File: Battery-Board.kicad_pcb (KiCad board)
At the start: 2 copper layers, 100 x 100 mm, 180 parts, among them IC2 ESDALC6V1W5, J11 OLED, J12 USB_C_Receptacle_USB2.0_16P, J13 STM32-Prog-Header, Q1 CSD18563Q5A, Q2 CSD18563Q5A, SW3 RESET, SW4 SW_SPDT, U1 8MHz, U10 NTMFS4D0N08XT1G, U11 NTMFS4D0N08XT1G, U12 NTMFS4D0N08XT1G, U13 NTMFS4D0N08XT1G, U14 NTMFS4D0N08XT1G, U23 ACS723xLCTR-10AU, U24 ACS723xLCTR-10AU, U25 MCP6007, U26 MCP6007, U27 ACS723xLCTR-10AU, U28 MCP6007, U29 MCP6007, U3 STM32G491KEUx, U30 MCP6007, U31 MCP6007, U4 MCP2542FD-E/SN, U5 MCP9700AT-ETT, U6 MCP9700AT-ETT, U7 MCP9700AT-ETT, U8 LM5145, U9 LM5145

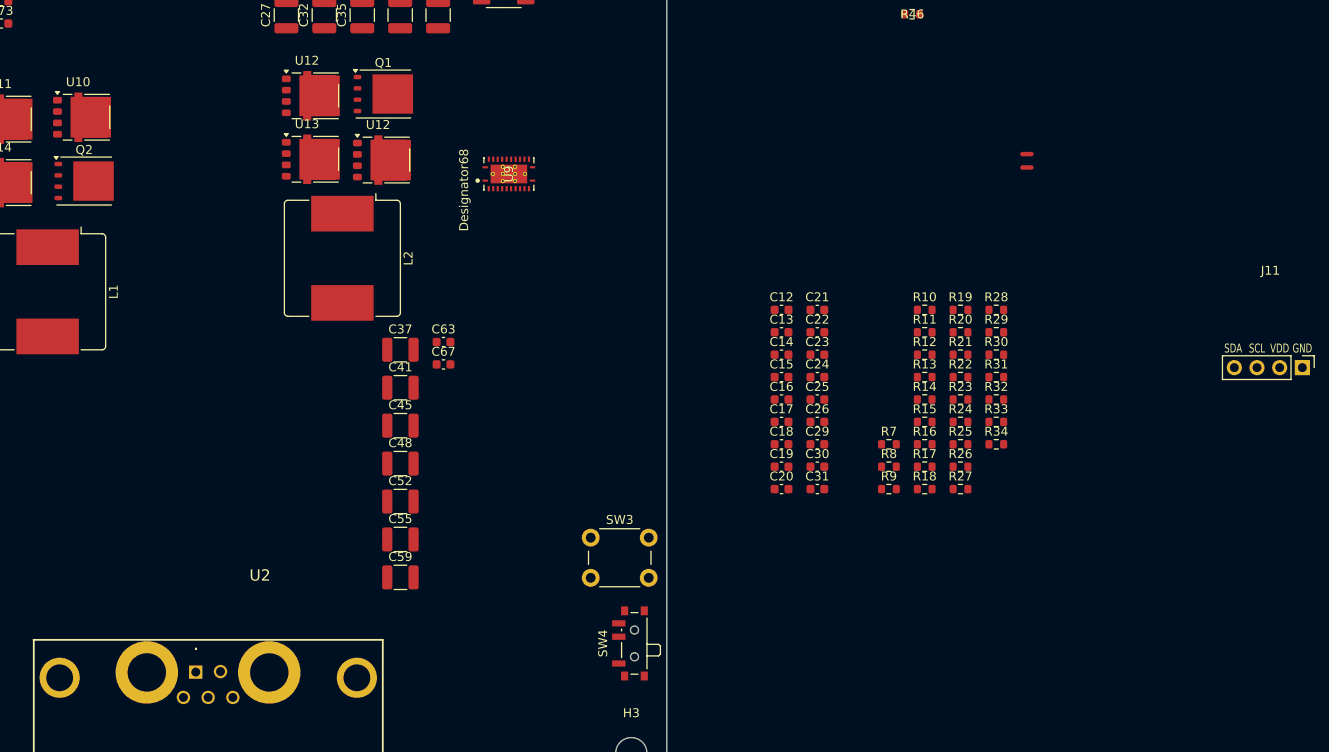
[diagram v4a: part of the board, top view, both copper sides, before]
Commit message: started sorting and cleaning up schemativc
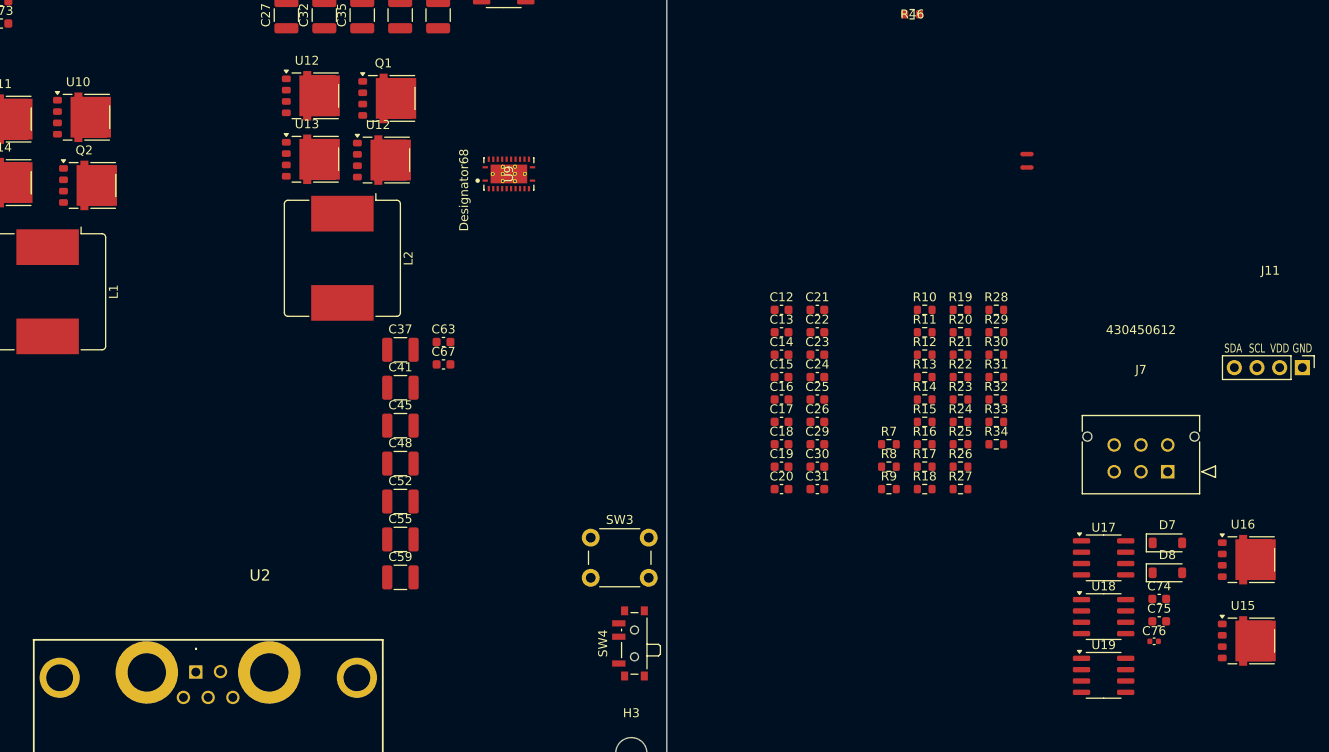
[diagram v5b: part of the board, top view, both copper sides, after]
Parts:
- added C74: 100n, Capacitor_SMD:C_0603_1608Metric, F.Cu at (243.0, 122.4)
- added C75: 1u5, Capacitor_SMD:C_0603_1608Metric, F.Cu at (243.0, 124.9)
- added C76: 1n, Capacitor_SMD:C_0402_1005Metric, F.Cu at (242.5, 127.2)
- added D7: MMSZ5226B-7-F, Diode_SMD:D_SOD-123, F.Cu at (244.0, 116.1)
- added D8: MMSZ5226B-7-F, Diode_SMD:D_SOD-123, F.Cu at (244.0, 119.5)
- added J7: STD_PWR_HEADER, ecocad_lib_footprints:CON_430450612_MOL, F.Cu at (244.0, 108.2)
- added U15: NTMFS4D0N08XT1G, ecocad_lib_footprints:PowerMosDFNHybrid, F.Cu at (252.4, 126.6)
- added U16: NTMFS4D0N08XT1G, ecocad_lib_footprints:PowerMosDFNHybrid, F.Cu at (252.4, 117.5)
- added U17: ACS723xLCTR-10AU, Package_SO:SOIC-8_3.9x4.9mm_P1.27mm, F.Cu at (236.8, 117.8)
- added U18: MCP6007, Package_SO:SOIC-8_3.9x4.9mm_P1.27mm, F.Cu at (236.8, 124.4)
- added U19: MCP6007, Package_SO:SOIC-8_3.9x4.9mm_P1.27mm, F.Cu at (236.8, 131.0)
- Q1, Q2: value CSD18563Q5A -> NTMFS4D0N08XT1G; footprint Package_TO_SOT_SMD:TDSON-8-1 -> ecocad_lib_footprints:PowerMosDFNHybrid
- R23: value 680 -> 680R
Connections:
- net /Power Circuitry/12V_Current_Out renamed /Power Sensors/12V_Current_Out
- net /Power Circuitry/12V_PCBs renamed /Power Sensors/12V_PCBs
- net /Power Circuitry/12V_Unsensed renamed /Power Sensors/12V_Unsensed
- net /Power Circuitry/7V_Current_Out renamed /Power Sensors/7V_Current_Out
- net /Power Circuitry/7V_PCBs renamed /Power Sensors/7V_PCBs
- net /Power Circuitry/7V_Unsensed renamed /Power Sensors/7V_Unsensed
- net /Power Circuitry/ADC_BUCK_12V_OUT renamed /Power Sensors/ADC_BUCK_12V_OUT
- net /Power Circuitry/ADC_BUCK_7V_Out renamed /Power Sensors/ADC_BUCK_7V_Out
- net /Power Circuitry/ADC_Battery_Voltage renamed /Power Sensors/ADC_Battery_Voltage
- net /Power Circuitry/Battery_Crrnt renamed /Power Sensors/Battery_Crrnt
- net /Power Circuitry/Battery_Terminal renamed /Power Sensors/Battery_Terminal
- net /Power Circuitry/Battery_Terminal_Unsensed renamed /Power Sensors/Battery_Terminal_Unsensed
- net /Power Circuitry/u11_unused renamed /Power Sensors/u11_unused
- net /Powerboard/SYNCOUT renamed /DC-DC-Converters/SYNCOUT
- net Net-(Q2-G) renamed /DC-DC-Converters/24V - 12V Converter/High Side Gate Drive
- net Net-(U11-G) renamed /DC-DC-Converters/24V - 12V Converter/Low Side Gate Drive
- C20 pad 1: GNDPWR -> GND
- C26 pad 2: GNDPWR -> GND
- C28 pad 1: +18.5V -> /DC-DC-Converters/24V - 12V Converter/POWER_IN
- C28 pad 2: GNDPWR -> GND
- C33 pad 1: +18.5V -> /DC-DC-Converters/24V - 12V Converter/POWER_IN
- C33 pad 2: GNDPWR -> GND
- C34 pad 1: Net-(C34-Pad1) -> /DC-DC-Converters/24V - 12V Converter/Output
- C34 pad 2: GNDPWR -> GND
- C36 pad 1: +18.5V -> /DC-DC-Converters/24V - 12V Converter/POWER_IN
- C36 pad 2: GNDPWR -> GND
- C38 pad 1: Net-(C34-Pad1) -> /DC-DC-Converters/24V - 12V Converter/Output
- C38 pad 2: GNDPWR -> GND
- C40 pad 1: +18.5V -> /DC-DC-Converters/24V - 12V Converter/POWER_IN
- C40 pad 2: GNDPWR -> GND
- C42 pad 1: Net-(C34-Pad1) -> /DC-DC-Converters/24V - 12V Converter/Output
- C42 pad 2: GNDPWR -> GND
- C44 pad 1: +18.5V -> /DC-DC-Converters/24V - 12V Converter/POWER_IN
- C44 pad 2: GNDPWR -> GND
- C46 pad 1: Net-(C34-Pad1) -> /DC-DC-Converters/24V - 12V Converter/Output
- C46 pad 2: GNDPWR -> GND
- C49 pad 1: +18.5V -> /DC-DC-Converters/24V - 12V Converter/POWER_IN
- C49 pad 2: GNDPWR -> GND
- C50 pad 1: Net-(C34-Pad1) -> /DC-DC-Converters/24V - 12V Converter/Output
- C50 pad 2: GNDPWR -> GND
- C53 pad 1: +18.5V -> /DC-DC-Converters/24V - 12V Converter/POWER_IN
- C53 pad 2: GNDPWR -> GND
- C54 pad 1: Net-(C34-Pad1) -> /DC-DC-Converters/24V - 12V Converter/Output
- C54 pad 2: GNDPWR -> GND
- C57 pad 1: Net-(C34-Pad1) -> /DC-DC-Converters/24V - 12V Converter/Output
- C57 pad 2: GNDPWR -> GND
- C58 pad 1: +18.5V -> /DC-DC-Converters/24V - 12V Converter/POWER_IN
- C58 pad 2: GNDPWR -> GND
- C61 pad 1: Net-(C34-Pad1) -> /DC-DC-Converters/24V - 12V Converter/Output
- C61 pad 2: GNDPWR -> GND
- C62 pad 1: +18.5V -> /DC-DC-Converters/24V - 12V Converter/POWER_IN
- C62 pad 2: GNDPWR -> GND
- C65 pad 1: Net-(C34-Pad1) -> /DC-DC-Converters/24V - 12V Converter/Output
- C65 pad 2: GNDPWR -> GND
- C66 pad 1: +18.5V -> /DC-DC-Converters/24V - 12V Converter/POWER_IN
- C66 pad 2: GNDPWR -> GND
- C69 pad 1: +18.5V -> /DC-DC-Converters/24V - 12V Converter/POWER_IN
- C69 pad 2: GNDPWR -> GND
- C71 pad 1: +18.5V -> /DC-DC-Converters/24V - 12V Converter/POWER_IN
- C71 pad 2: GNDPWR -> GND
- C73 pad 1: +18.5V -> /DC-DC-Converters/24V - 12V Converter/POWER_IN
- C73 pad 2: GNDPWR -> GND
- L1 pad 2: Net-(C34-Pad1) -> Net-(L1-Pad2)
- Q2 pad 1: +18.5V -> Net-(Q2-S-Pad1)
- Q2 pad 2: +18.5V -> Net-(Q2-S-Pad1)
- Q2 pad 3: +18.5V -> Net-(Q2-S-Pad1)
- R17 pad 1: +18.5V -> Net-(Q2-S-Pad1)
- R33 pad 2: Net-(C34-Pad1) -> Net-(L1-Pad2)
- R9 pad 1: +18.5V -> Net-(Q2-S-Pad1)
- U10 pad 1: +18.5V -> Net-(Q2-S-Pad1)
- U10 pad 2: +18.5V -> Net-(Q2-S-Pad1)
- U10 pad 3: +18.5V -> Net-(Q2-S-Pad1)
- U11 pad 5: GNDPWR -> GND
- U12 pad 1: (no net) -> +18.5V
- U12 pad 2: (no net) -> +18.5V
- U12 pad 3: (no net) -> +18.5V
- U12 pad 4: (no net) -> Net-(U12-G)
- U12 pad 5: (no net) -> Net-(Q1-D)
- U14 pad 5: GNDPWR -> GND

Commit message: Started Layout and cleaned up schematic
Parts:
- removed C43, C44, C46, C47, C49, C50, C51, C53, C54, C56, C57, C58: 10u, Capacitor_SMD:C_1210_3225Metric
- removed C45, C48, C52, C55, C59: 47u, Capacitor_SMD:C_1210_3225Metric
- removed C60, C62, C64, C66, C68, C69, C70, C71, C72, C73: 100n, Capacitor_SMD:C_0603_1608Metric
- removed C61, C63, C65, C67: 220u, Capacitor_SMD:C_0603_1608Metric
- removed D13, D14, D15, D16, D17, D18: MMSZ5226B-7-F, Diode_SMD:D_SOD-123
- removed FB2: 600@100MHz 1A, Inductor_SMD:L_0603_1608Metric
- removed IC2: ESDALC6V1W5, ecocad_lib_footprints:SOT65P210X110-5N
- removed J11: OLED, ecocad_lib_footprints:Display_128x64_096_I2C
- removed J12: USB_C_Receptacle_USB2.0_16P, Connector_USB:USB_C_Receptacle_GCT_USB4105-xx-A_16P_TopMnt_Horizontal
- removed J13: STM32-Prog-Header, ecocad_lib_footprints:IDC-STM32-Prog-Header_2x05_P2.54mm_Vertical
- removed J7: STD_PWR_HEADER, ecocad_lib_footprints:CON_430450612_MOL
- removed L2: 12u, ecocad_lib_footprints:L_Bourns_SRR1208_12.7x12.7mm
- removed NT1, NT2: NetTie_2, NetTie:NetTie-2_SMD_Pad0.5mm
- removed Q1, Q2, U13, U14, U15, U16: NTMFS4D0N08XT1G, ecocad_lib_footprints:PowerMosDFNHybrid
- removed R22: 0, Resistor_SMD:R_0603_1608Metric
- removed R23: 680R, Resistor_SMD:R_0603_1608Metric
- removed R24: 422, Resistor_SMD:R_0603_1608Metric
- removed R25: 3.83k, Resistor_SMD:R_0603_1608Metric
- removed R26: 3.3k, Resistor_SMD:R_0603_1608Metric
- removed R27, R28: 10k, Resistor_SMD:R_0603_1608Metric
- removed R29: 14k, Resistor_SMD:R_0603_1608Metric
- removed R30: 7.75k, Resistor_SMD:R_0603_1608Metric
- removed R31, R32: 1.00k, Resistor_SMD:R_0603_1608Metric
- removed R33, R34: 49.9, Resistor_SMD:R_0603_1608Metric
- removed SW3: RESET, Button_Switch_THT:SW_PUSH_6mm_H5mm
- removed SW4: SW_SPDT, Button_Switch_SMD:SW_SPDT_PCM12
- removed the U12 at (147.6, 65.6)
- removed the U12 at (155.5, 72.8)
- removed U24, U27: ACS723xLCTR-10AU, Package_SO:SOIC-8_3.9x4.9mm_P1.27mm
- removed U25, U26, U28, U29, U30, U31: MCP6007, Package_SO:SOIC-8_3.9x4.9mm_P1.27mm
- added C100: 15pF, Capacitor_SMD:C_0603_1608Metric, F.Cu at (111.2, 99.6)
- added C101: 150pF, Capacitor_SMD:C_0603_1608Metric, F.Cu at (118.5, 88.9)
- added C102: 100n, Capacitor_SMD:C_0603_1608Metric, F.Cu at (137.2, 101.8)
- added C104: 100n, Capacitor_SMD:C_0603_1608Metric, F.Cu at (135.6, 112.4)
- added C105: 1800pF, Capacitor_SMD:C_0603_1608Metric, F.Cu at (112.3, 88.9)
- added C106: 100n, Capacitor_SMD:C_0603_1608Metric, F.Cu at (134.1, 112.4)
- added C107: 100n, Capacitor_SMD:C_0603_1608Metric, F.Cu at (115.9, 99.0)
- added C77: 100n, Capacitor_SMD:C_0603_1608Metric, F.Cu at (78.3, 107.1)
- added C78: 10u, Capacitor_SMD:C_1210_3225Metric, F.Cu at (131.7, 101.0)
- added C79: 10u, Capacitor_SMD:C_1210_3225Metric, F.Cu at (131.5, 113.2)
- added C80: 100u, Capacitor_SMD:C_1210_3225Metric, F.Cu at (118.2, 119.5)
- added C81: 10u, Capacitor_SMD:C_1210_3225Metric, F.Cu at (128.2, 113.2)
- added C82: 1u, Capacitor_SMD:C_0603_1608Metric, F.Cu at (107.6, 85.8)
- added C83: 100n, Capacitor_SMD:C_0603_1608Metric, F.Cu at (122.3, 96.5)
- added C84: 100u, Capacitor_SMD:C_1210_3225Metric, F.Cu at (121.5, 119.5)
- added C97: 100n, Capacitor_SMD:C_0603_1608Metric, F.Cu at (135.7, 101.8)
- added C98: 5600pF, Capacitor_SMD:C_0603_1608Metric, F.Cu at (117.0, 88.9)
- added C99: 220u, ecocad_lib_footprints:CAP_EEE1HA221P, F.Cu at (104.5, 140.8)
- added FB1: 600@100MHz 1A, Inductor_SMD:L_0603_1608Metric, F.Cu at (58.2, 59.9)
- added IC1: ESDALC6V1W5, ecocad_lib_footprints:SOT65P210X110-5N, F.Cu at (24.6, 64.4)
- added J1: OLED, ecocad_lib_footprints:Display_128x64_096_I2C, F.Cu at (40.5, 30.5)
- added J2: USB_C_Receptacle_USB2.0_16P, Connector_USB:USB_C_Receptacle_GCT_USB4105-xx-A_16P_TopMnt_Horizontal, F.Cu at (172.0, 145.9)
- added J3: STM32-Prog-Header, Connector_PinHeader_2.54mm:PinHeader_2x05_P2.54mm_Vertical, F.Cu at (185.7, 56.1)
- added J4: Conn_01x01_Socket, Connector_PinHeader_2.54mm:PinHeader_1x01_P2.54mm_Vertical, F.Cu at (215.5, 86.5)
- added J5: Conn_01x01_Socket, Connector_PinHeader_2.54mm:PinHeader_1x01_P2.54mm_Vertical, F.Cu at (109.9, 82.2)
- added L3: 6u8, ecocad_lib_footprints:L_Bourns_SRR1208_12.7x12.7mm, F.Cu at (109.5, 121.6)
- added R36: 18.2k, Resistor_SMD:R_0603_1608Metric, F.Cu at (122.3, 91.9)
- added R37: 250k, Resistor_SMD:R_0603_1608Metric, F.Cu at (122.3, 93.5)
- added R38: 10k, Resistor_SMD:R_0603_1608Metric, F.Cu at (109.2, 88.9)
- added R39: 46.4k, Resistor_SMD:R_0603_1608Metric, F.Cu at (121.6, 88.9)
- added R40: 10k, Resistor_SMD:R_0603_1608Metric, F.Cu at (107.6, 88.9)
- added R49: 1.00k, Resistor_SMD:R_0603_1608Metric, F.Cu at (113.1, 86.6)
- added R50: 49.9, Resistor_SMD:R_0603_1608Metric, F.Cu at (113.1, 85.0)
- added SW1: RESET, Button_Switch_THT:SW_PUSH_6mm_H5mm, F.Cu at (56.1, 30.2)
- added SW2: SW_SPDT, Button_Switch_SMD:SW_SPDT_PCM12, F.Cu at (59.0, 39.7)
- added U12: MCP9700AT-ETT, Package_TO_SOT_SMD:SOT-23, F.Cu at (45.7, 67.8)
- added U20: NTMFS4D0N08XT1G, ecocad_lib_footprints:PowerMosDFNHybrid, F.Cu at (115.7, 109.8)
- added U21: NTMFS4D0N08XT1G, ecocad_lib_footprints:PowerMosDFNHybrid, F.Cu at (108.3, 109.8)
- added U22: NTMFS4D0N08XT1G, ecocad_lib_footprints:PowerMosDFNHybrid, F.Cu at (115.7, 103.4)
- C1, C15, C2, C85, C92: value 100n -> 10u; footprint Capacitor_SMD:C_0603_1608Metric -> Capacitor_SMD:C_1210_3225Metric
- C10, C14, C19, C7, C91, C96: value 100n -> 100u; footprint Capacitor_SMD:C_0603_1608Metric -> Capacitor_SMD:C_1210_3225Metric
- C11, C4, C8: value 0u1 -> 10u; footprint Capacitor_SMD:C_0603_1608Metric -> Capacitor_SMD:C_1210_3225Metric
- C12, C87: value 1u -> 100u; footprint Capacitor_SMD:C_0603_1608Metric -> Capacitor_SMD:C_1210_3225Metric
- C13: value 1u -> 10u; footprint Capacitor_SMD:C_0603_1608Metric -> Capacitor_SMD:C_1210_3225Metric
- C16: value 47n -> 10u; footprint Capacitor_SMD:C_0603_1608Metric -> Capacitor_SMD:C_1210_3225Metric
- C17: value 47n -> 100u; footprint Capacitor_SMD:C_0603_1608Metric -> Capacitor_SMD:C_1210_3225Metric
- C20: value 15pF -> 100n
- C21: value 15pF -> 5600pF
- C22: value 5600pF -> 220u; footprint Capacitor_SMD:C_0603_1608Metric -> ecocad_lib_footprints:CAP_EEE1HA221P
- C23: value 5600pF -> 15pF
- C25: value 150pF -> 100n
- C26: value 15n -> 220u; footprint Capacitor_SMD:C_0603_1608Metric -> ecocad_lib_footprints:CAP_EEE1HA221P
- C27, C32, C33, C38: value 10u -> 100n; footprint Capacitor_SMD:C_1210_3225Metric -> Capacitor_SMD:C_0603_1608Metric
- C28: value 10u -> 1800pF; footprint Capacitor_SMD:C_1210_3225Metric -> Capacitor_SMD:C_0603_1608Metric
- C29, C30: value 1800pF -> 100n
- C3: value 0u1 -> 100u; footprint Capacitor_SMD:C_0603_1608Metric -> Capacitor_SMD:C_1210_3225Metric
- C31: value C -> 220u; footprint Capacitor_SMD:C_0603_1608Metric -> ecocad_lib_footprints:CAP_EEE1HA221P
- C34, C35, C39, C42: value 10u -> 0u1; footprint Capacitor_SMD:C_1210_3225Metric -> Capacitor_SMD:C_0603_1608Metric
- C36: value 10u -> 4u7; footprint Capacitor_SMD:C_1210_3225Metric -> Capacitor_SMD:C_0603_1608Metric
- C37: value 47u -> 4u7; footprint Capacitor_SMD:C_1210_3225Metric -> Capacitor_SMD:C_0603_1608Metric
- C40: value 10u -> 1u; footprint Capacitor_SMD:C_1210_3225Metric -> Capacitor_SMD:C_0603_1608Metric
- C41: value 47u -> 100n; footprint Capacitor_SMD:C_1210_3225Metric -> Capacitor_SMD:C_0603_1608Metric
- C5: value 4u7 -> 1u
- C6: value 4u7 -> 100n
- C86: value 100n -> 47n
- C88: value 6.8u -> 10u; footprint Capacitor_SMD:C_0603_1608Metric -> Capacitor_SMD:C_1210_3225Metric
- C89, C94: value 1n -> 100u; footprint Capacitor_SMD:C_0402_1005Metric -> Capacitor_SMD:C_1210_3225Metric
- C9: value 1u -> 47n
- C90: value 1n -> 10u; footprint Capacitor_SMD:C_0402_1005Metric -> Capacitor_SMD:C_1210_3225Metric
- C93: value 1u5 -> 10u; footprint Capacitor_SMD:C_0603_1608Metric -> Capacitor_SMD:C_1210_3225Metric
- L1: value 6.8u -> 6u8
- R1: value 220R -> 18.2k; footprint Resistor_SMD:R_0805_2012Metric -> Resistor_SMD:R_0603_1608Metric
- R10: value 301k -> 3.83k
- R11: value 46.4k -> 10k
- R12: value 46.4k -> 0
- R13: value 20.0k -> 14k
- R14: value 20.0k -> 1.00k
- R15: value 20.0k -> 49.9
- R16: value 20.0k -> 220R; footprint Resistor_SMD:R_0603_1608Metric -> Resistor_SMD:R_0805_2012Metric
- R17: value 2.2 -> 220R; footprint Resistor_SMD:R_0603_1608Metric -> Resistor_SMD:R_0805_2012Metric
- R18: value 4.7 -> 220R; footprint Resistor_SMD:R_0603_1608Metric -> Resistor_SMD:R_0805_2012Metric
- R19: value 0 -> R
- R2: value 220R -> 250k; footprint Resistor_SMD:R_0805_2012Metric -> Resistor_SMD:R_0603_1608Metric
- R20, R21: value 0 -> 5.1k; footprint Resistor_SMD:R_0603_1608Metric -> Resistor_SMD:R_0805_2012Metric
- R3: value 220R -> 10k; footprint Resistor_SMD:R_0805_2012Metric -> Resistor_SMD:R_0603_1608Metric
- R4: value R -> 46.4k
- R41: value 28k7 -> 20.0k
- R42: value 10k -> 2.2
- R43: value 4k7 -> 680R
- R44: value 1k02 -> 0
- R45: value 13k6 -> 3.83k
- R46: value 4k7 -> 10k
- R47: value 47k -> 0; footprint Resistor_SMD:R_0805_2012Metric -> Resistor_SMD:R_0603_1608Metric
- R48: value 47k -> 14k; footprint Resistor_SMD:R_0805_2012Metric -> Resistor_SMD:R_0603_1608Metric
- R5: value 5.1k -> 10k; footprint Resistor_SMD:R_0805_2012Metric -> Resistor_SMD:R_0603_1608Metric
- R6: value 5.1k -> 20.0k; footprint Resistor_SMD:R_0805_2012Metric -> Resistor_SMD:R_0603_1608Metric
- R7: value 18.2k -> 2.2
- R8: value 18.2k -> 680R
- R9: value 250k -> 0
- U1: value 8MHz -> LM5145; footprint Crystal:Crystal_SMD_3225-4Pin_3.2x2.5mm -> Package_DFN_QFN:Texas_RGY_R-PVQFN-N20_EP2.05x3.05mm_ThermalVias
- U10, U11: value NTMFS4D0N08XT1G -> MCP9700AT-ETT; footprint ecocad_lib_footprints:PowerMosDFNHybrid -> Package_TO_SOT_SMD:SOT-23
- U19: value MCP6007 -> LM5145; footprint Package_SO:SOIC-8_3.9x4.9mm_P1.27mm -> Package_DFN_QFN:Texas_RGY_R-PVQFN-N20_EP2.05x3.05mm_ThermalVias
- U2: value ~ -> NTMFS4D0N08XT1G; footprint ecocad_lib_footprints:DB7W2-30A -> ecocad_lib_footprints:PowerMosDFNHybrid
- U23: value ACS723xLCTR-10AU -> NTMFS4D0N08XT1G; footprint Package_SO:SOIC-8_3.9x4.9mm_P1.27mm -> ecocad_lib_footprints:PowerMosDFNHybrid
- U3: value STM32G491KEUx -> NTMFS4D0N08XT1G; footprint Package_DFN_QFN:QFN-32-1EP_5x5mm_P0.5mm_EP3.45x3.45mm -> ecocad_lib_footprints:PowerMosDFNHybrid
- U4: value MCP2542FD-E/SN -> NTMFS4D0N08XT1G; footprint Package_SO:SOIC-8_3.9x4.9mm_P1.27mm -> ecocad_lib_footprints:PowerMosDFNHybrid
- U5: value MCP9700AT-ETT -> NTMFS4D0N08XT1G; footprint Package_TO_SOT_SMD:SOT-23 -> ecocad_lib_footprints:PowerMosDFNHybrid
- U6: value MCP9700AT-ETT -> 8MHz; footprint Package_TO_SOT_SMD:SOT-23 -> Crystal:Crystal_SMD_3225-4Pin_3.2x2.5mm
- U7: value MCP9700AT-ETT -> ~; footprint Package_TO_SOT_SMD:SOT-23 -> ecocad_lib_footprints:DB7W2-Female
- U8: value LM5145 -> STM32G491KEUx; footprint ecocad_lib_footprints:RGY0024F-MFG -> Package_DFN_QFN:QFN-32-1EP_5x5mm_P0.5mm_EP3.45x3.45mm
- U9: value LM5145 -> MCP2542FD-E/SN; footprint ecocad_lib_footprints:RGY0024F-MFG -> Package_SO:SOIC-8_3.9x4.9mm_P1.27mm
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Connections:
- C1 pad 1: GNDA -> /DC-DC-Converters/24V - 7V Converter/POWER_IN
- C1 pad 2: +3V3 -> GND
- C10 pad 1: GND -> /DC-DC-Converters/24V - 7V Converter/Output
- C10 pad 2: +3V3 -> GND
- C11 pad 1: +3V3 -> /DC-DC-Converters/24V - 7V Converter/POWER_IN
- C12 pad 1: GND -> /DC-DC-Converters/24V - 7V Converter/Output
- C12 pad 2: Net-(U8-VCC) -> GND
- C13 pad 1: GND -> /DC-DC-Converters/24V - 7V Converter/POWER_IN
- C13 pad 2: Net-(U9-VCC) -> GND
- C14 pad 1: GNDPWR -> /DC-DC-Converters/24V - 7V Converter/Output
- C14 pad 2: Net-(U8-VIN) -> GND
- C15 pad 1: GNDPWR -> /DC-DC-Converters/24V - 7V Converter/POWER_IN
- C15 pad 2: Net-(U9-VIN) -> GND
- C16 pad 1: GND -> /DC-DC-Converters/24V - 7V Converter/POWER_IN
- C16 pad 2: Net-(U8-SS_TRK) -> GND
- C17 pad 1: GND -> /DC-DC-Converters/24V - 7V Converter/Output
- C17 pad 2: Net-(U9-SS_TRK) -> GND
- C18 pad 1: Net-(Q2-D) -> /DC-DC-Converters/24V - 7V Converter/POWER_IN
- C18 pad 2: Net-(Q2-D) -> GND
- C19 pad 1: Net-(Q1-D) -> /DC-DC-Converters/24V - 7V Converter/Output
- C19 pad 2: Net-(Q1-D) -> GND
- C2 pad 1: GND -> /DC-DC-Converters/24V - 7V Converter/POWER_IN
- C2 pad 2: /MCU and sensors/NRST -> GND
- C20 pad 1: GND -> /DC-DC-Converters/24V - 7V Converter/POWER_IN
- C20 pad 2: Net-(U8-ILIM) -> GND
- C21 pad 1: GNDPWR -> Net-(U1-COMP)
- C21 pad 2: Net-(U9-ILIM) -> Net-(C21-Pad2)
- C22 pad 1: Net-(U8-COMP) -> /DC-DC-Converters/24V - 7V Converter/Output
- C22 pad 2: Net-(C22-Pad2) -> GND
- C23 pad 1: Net-(U9-COMP) -> GND
- C23 pad 2: Net-(C23-Pad2) -> Net-(U1-ILIM)
- C24 pad 1: Net-(U8-COMP) -> Net-(U1-COMP)
- C24 pad 2: Net-(U8-FB) -> Net-(U1-FB)
- C25 pad 1: Net-(U9-COMP) -> /DC-DC-Converters/24V - 7V Converter/POWER_IN
- C25 pad 2: Net-(U9-FB) -> GND
- C26 pad 1: Net-(Q2-D) -> /DC-DC-Converters/24V - 7V Converter/Output
- C27 pad 1: +18.5V -> /DC-DC-Converters/24V - 7V Converter/POWER_IN
- C27 pad 2: GNDPWR -> GND
- C28 pad 1: /DC-DC-Converters/24V - 12V Converter/POWER_IN -> Net-(U1-FB)
- C28 pad 2: GND -> Net-(C28-Pad2)
- C29 pad 1: Net-(U8-FB) -> /DC-DC-Converters/24V - 7V Converter/POWER_IN
- C29 pad 2: Net-(C29-Pad2) -> GND
- C3 pad 1: +3V3 -> /DC-DC-Converters/24V - 7V Converter/Output
- C3 pad 2: GNDA -> GND
- C30 pad 1: Net-(U9-FB) -> Net-(U1-SW)
- C30 pad 2: Net-(C30-Pad2) -> Net-(U1-BST)
- C31 pad 1: Net-(Q1-D) -> /DC-DC-Converters/24V - 12V Converter/Output
- C31 pad 2: GNDPWR -> GND
- C32 pad 1: +18.5V -> GNDA
- C32 pad 2: GNDPWR -> +3V3
- C33 pad 1: /DC-DC-Converters/24V - 12V Converter/POWER_IN -> GND
- C33 pad 2: GND -> /MCU and sensors/NRST
- C34 pad 1: /DC-DC-Converters/24V - 12V Converter/Output -> +3V3
- C34 pad 2: GND -> GNDA
- C35 pad 1: +18.5V -> +3V3
- C35 pad 2: GNDPWR -> GNDA
- C36 pad 1: /DC-DC-Converters/24V - 12V Converter/POWER_IN -> +3V3
- C36 pad 2: GND -> GNDA
- C37 pad 1: Net-(C37-Pad1) -> +3.3VA
- C37 pad 2: GNDPWR -> unconnected-(C37-Pad2)
- C38 pad 1: /DC-DC-Converters/24V - 12V Converter/Output -> GND
- C38 pad 2: GND -> +5V
- C39 pad 1: +18.5V -> +3.3VA
- C39 pad 2: GNDPWR -> GND
- C4 pad 1: +3V3 -> /DC-DC-Converters/24V - 7V Converter/POWER_IN
- C4 pad 2: GNDA -> GND
- C40 pad 1: /DC-DC-Converters/24V - 12V Converter/POWER_IN -> +3.3VA
- C41 pad 1: Net-(C37-Pad1) -> GND
- C41 pad 2: GNDPWR -> +3V3
- C42 pad 1: /DC-DC-Converters/24V - 12V Converter/Output -> +3V3
- C5 pad 1: +3V3 -> GND
- C5 pad 2: GNDA -> Net-(U1-VCC)
- C6 pad 1: +3.3VA -> GND
- C6 pad 2: unconnected-(C6-Pad2) -> Net-(U1-VIN)
- C7 pad 1: GND -> /DC-DC-Converters/24V - 7V Converter/Output
- C7 pad 2: +5V -> GND
- C74 pad 2: GND -> /Power Sensor VI/SENSOR_GND
- C8 pad 1: +3.3VA -> /DC-DC-Converters/24V - 7V Converter/POWER_IN
- C85 pad 1: +5V -> /DC-DC-Converters/24V - 12V Converter/POWER_IN
- C86 pad 2: +5V -> Net-(U19-SS_TRK)
- C87 pad 1: Net-(D13-K) -> /DC-DC-Converters/24V - 12V Converter/Output
- C88 pad 1: Net-(D14-K) -> /DC-DC-Converters/24V - 12V Converter/POWER_IN
- C89 pad 1: Net-(D15-K) -> /DC-DC-Converters/24V - 12V Converter/Output
- C9 pad 1: +3.3VA -> GND
- C9 pad 2: GND -> Net-(U1-SS_TRK)
- C90 pad 1: Net-(D16-K) -> /DC-DC-Converters/24V - 12V Converter/POWER_IN
- C91 pad 1: +5V -> /DC-DC-Converters/24V - 12V Converter/Output
- C92 pad 1: +5V -> /DC-DC-Converters/24V - 12V Converter/POWER_IN
- C93 pad 1: Net-(D17-K) -> /DC-DC-Converters/24V - 12V Converter/POWER_IN
- C94 pad 1: Net-(D18-K) -> /DC-DC-Converters/24V - 12V Converter/Output
- C95 pad 1: +5V -> /DC-DC-Converters/24V - 12V Converter/POWER_IN
- C96 pad 1: +5V -> /DC-DC-Converters/24V - 12V Converter/Output
- L1 pad 1: Net-(Q2-D) -> Net-(U1-SW)
- L1 pad 2: Net-(L1-Pad2) -> /DC-DC-Converters/24V - 7V Converter/Output
- R1 pad 1: Net-(D1-A) -> GND
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
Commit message: A
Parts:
- added C43: 100u, Capacitor_SMD:C_1210_3225Metric, F.Cu at (236.8, 133.8)
- added C44: 100u, Capacitor_SMD:C_1210_3225Metric, B.Cu at (118.1, 119.5)
- C1, C11, C13, C15, C16, C2, C4, C78, C79, C8, C81, C85, C88, C90, C92, C93: value 10u -> 100u
- C91, C94, C96: moved to B.Cu
- moved C96 16.6 mm to (121.4, 119.5)
- moved C94 9.93 mm to (124.8, 119.5)
- moved C91 3.32 mm to (128.1, 119.5)

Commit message: A
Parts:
- removed C100: 15pF, Capacitor_SMD:C_0603_1608Metric
- removed C101: 150pF, Capacitor_SMD:C_0603_1608Metric
- removed C102, C104, C106, C107, C95, C97: 100n, Capacitor_SMD:C_0603_1608Metric
- removed C105: 1800pF, Capacitor_SMD:C_0603_1608Metric
- removed C94, C96: 100u, Capacitor_SMD:C_1210_3225Metric
- removed C98: 5600pF, Capacitor_SMD:C_0603_1608Metric
- removed C99: 220u, ecocad_lib_footprints:CAP_EEE1HA221P
- removed L3: 6u8, ecocad_lib_footprints:L_Bourns_SRR1208_12.7x12.7mm
- removed R36: 18.2k, Resistor_SMD:R_0603_1608Metric
- removed R37: 250k, Resistor_SMD:R_0603_1608Metric
- removed R38, R40, R46: 10k, Resistor_SMD:R_0603_1608Metric
- removed R39: 46.4k, Resistor_SMD:R_0603_1608Metric
- removed R41: 20.0k, Resistor_SMD:R_0603_1608Metric
- removed R42: 2.2, Resistor_SMD:R_0603_1608Metric
- removed R43: 680R, Resistor_SMD:R_0603_1608Metric
- removed R44, R47: 0, Resistor_SMD:R_0603_1608Metric
- removed R45: 3.83k, Resistor_SMD:R_0603_1608Metric
- removed R48: 14k, Resistor_SMD:R_0603_1608Metric
- removed R49: 1.00k, Resistor_SMD:R_0603_1608Metric
- removed R50: 49.9, Resistor_SMD:R_0603_1608Metric
- added C45: 100n, Capacitor_SMD:C_0603_1608Metric, F.Cu at (18.9, 117.2)
- added C46: 220u, ecocad_lib_footprints:CAP_EEE1HA221P, F.Cu at (24.1, 136.9)
- added C47: 100n, Capacitor_SMD:C_0603_1608Metric, F.Cu at (18.9, 119.7)
- added C48: 1800pF, Capacitor_SMD:C_0603_1608Metric, F.Cu at (18.9, 122.2)
- added C49: 100n, Capacitor_SMD:C_0603_1608Metric, F.Cu at (18.9, 124.7)
- added C50: 100n, Capacitor_SMD:C_0603_1608Metric, F.Cu at (18.9, 127.2)
- added C51: 100n, Capacitor_SMD:C_0603_1608Metric, F.Cu at (49.9, 85.9)
- added C52: 1u5, Capacitor_SMD:C_0603_1608Metric, F.Cu at (49.9, 88.4)
- added C53: 1n, Capacitor_SMD:C_0402_1005Metric, F.Cu at (53.4, 92.3)
- added C54: 100n, Capacitor_SMD:C_0603_1608Metric, F.Cu at (49.9, 90.9)
- added C55: 100u, Capacitor_SMD:C_1210_3225Metric, F.Cu at (11.7, 86.7)
- added C56: 100u, Capacitor_SMD:C_1210_3225Metric, F.Cu at (11.7, 91.0)
- added C57: 100u, Capacitor_SMD:C_1210_3225Metric, F.Cu at (11.7, 95.2)
- added C58: 100u, Capacitor_SMD:C_1210_3225Metric, F.Cu at (11.7, 99.5)
- added C59: 100u, Capacitor_SMD:C_1210_3225Metric, F.Cu at (11.7, 103.7)
- added C60: 1u, Capacitor_SMD:C_0603_1608Metric, F.Cu at (27.8, 100.1)
- added C61: 100n, Capacitor_SMD:C_0603_1608Metric, F.Cu at (27.8, 102.6)
- added C62: 100u, Capacitor_SMD:C_1210_3225Metric, F.Cu at (11.7, 108.0)
- added C63: 100u, Capacitor_SMD:C_1210_3225Metric, F.Cu at (17.4, 86.7)
- added C64: 47n, Capacitor_SMD:C_0603_1608Metric, F.Cu at (27.8, 105.1)
- added C65: 100u, Capacitor_SMD:C_1210_3225Metric, F.Cu at (17.4, 91.0)
- added C66: 100u, Capacitor_SMD:C_1210_3225Metric, F.Cu at (17.4, 95.2)
- added C67: 100u, Capacitor_SMD:C_1210_3225Metric, F.Cu at (17.4, 99.5)
- added C68: 100u, Capacitor_SMD:C_1210_3225Metric, F.Cu at (17.4, 103.7)
- added C69: 100u, Capacitor_SMD:C_1210_3225Metric, F.Cu at (17.4, 108.0)
- added C70: 100u, Capacitor_SMD:C_1210_3225Metric, F.Cu at (23.0, 86.7)
- added C71: 100u, Capacitor_SMD:C_1210_3225Metric, F.Cu at (23.0, 91.0)
- added C72: 100u, Capacitor_SMD:C_1210_3225Metric, F.Cu at (23.0, 95.2)
- added C73: 100n, Capacitor_SMD:C_0603_1608Metric, F.Cu at (27.8, 107.6)
- added D10: MMSZ5226B-7-F, Diode_SMD:D_SOD-123, F.Cu at (50.8, 100.3)
- added D11: MMSZ5226B-7-F, Diode_SMD:D_SOD-123, F.Cu at (54.8, 86.3)
- added D12: MMSZ5226B-7-F, Diode_SMD:D_SOD-123, F.Cu at (54.8, 89.6)
- added D13: MMSZ5226B-7-F, Diode_SMD:D_SOD-123, F.Cu at (44.6, 117.6)
- added D14: MMSZ5226B-7-F, Diode_SMD:D_SOD-123, F.Cu at (44.6, 120.9)
- added D15: MMSZ5226B-7-F, Diode_SMD:D_SOD-123, F.Cu at (44.6, 132.8)
- added D16: MMSZ5226B-7-F, Diode_SMD:D_SOD-123, F.Cu at (44.6, 136.1)
- added D9: MMSZ5226B-7-F, Diode_SMD:D_SOD-123, F.Cu at (50.8, 97.0)
- added G***: LOGO, LOGO, F.Cu at (107.0, 68.6)
- added G***: LOGO, LOGO, F.Cu at (135.7, 116.6)
- added G***: LOGO, LOGO, F.Cu at (155.7, 79.0)
- added L2: 6u8, ecocad_lib_footprints:L_Bourns_SRR1208_12.7x12.7mm, F.Cu at (33.6, 91.7)
- added R22: 1.00k, Resistor_SMD:R_0603_1608Metric, F.Cu at (18.9, 129.7)
- added R23: 18.2k, Resistor_SMD:R_0603_1608Metric, F.Cu at (27.8, 110.2)
- added R24: 250k, Resistor_SMD:R_0603_1608Metric, F.Cu at (27.8, 112.7)
- added R25: 10k, Resistor_SMD:R_0603_1608Metric, F.Cu at (31.8, 100.1)
- added R26: 46.4k, Resistor_SMD:R_0603_1608Metric, F.Cu at (31.8, 102.6)
- added R27: 10k, Resistor_SMD:R_0603_1608Metric, F.Cu at (31.8, 105.1)
- added R28: 20.0k, Resistor_SMD:R_0603_1608Metric, F.Cu at (31.8, 107.6)
- added R29: 2.2, Resistor_SMD:R_0603_1608Metric, F.Cu at (31.8, 110.2)
- added R30: 680R, Resistor_SMD:R_0603_1608Metric, F.Cu at (31.8, 112.7)
- added R31: 0, Resistor_SMD:R_0603_1608Metric, F.Cu at (35.9, 100.1)
- added R32: 10k, Resistor_SMD:R_0603_1608Metric, F.Cu at (35.9, 102.6)
- added R33: 0, Resistor_SMD:R_0603_1608Metric, F.Cu at (35.9, 105.1)
- added R34: 1.00k, Resistor_SMD:R_0603_1608Metric, F.Cu at (35.9, 107.6)
- added U13: NTMFS4D0N08XT1G, ecocad_lib_footprints:PowerMosDFNHybrid, F.Cu at (12.5, 119.0)
- added U14: NTMFS4D0N08XT1G, ecocad_lib_footprints:PowerMosDFNHybrid, F.Cu at (12.5, 126.1)
- added U15: NTMFS4D0N08XT1G, ecocad_lib_footprints:PowerMosDFNHybrid, F.Cu at (12.5, 133.2)
- added U16: NTMFS4D0N08XT1G, ecocad_lib_footprints:PowerMosDFNHybrid, F.Cu at (12.5, 140.3)
- added U24: NTMFS4D0N08XT1G, ecocad_lib_footprints:PowerMosDFNHybrid, F.Cu at (41.5, 101.9)
- added U25: NTMFS4D0N08XT1G, ecocad_lib_footprints:PowerMosDFNHybrid, F.Cu at (41.5, 109.0)
- added U26: ACS723xLCTR-10AU, Package_SO:SOIC-8_3.9x4.9mm_P1.27mm, F.Cu at (37.5, 119.3)
- added U27: MCP6007, Package_SO:SOIC-8_3.9x4.9mm_P1.27mm, F.Cu at (37.5, 125.8)
- added U28: ACS723xLCTR-10AU, Package_SO:SOIC-8_3.9x4.9mm_P1.27mm, F.Cu at (37.5, 134.4)
- added U29: MCP6007, Package_SO:SOIC-8_3.9x4.9mm_P1.27mm, F.Cu at (37.5, 141.0)
- C1, C11, C14, C16, C19, C4, C80, C84, C85, C89, C90, C93: value 100u -> 100n; footprint Capacitor_SMD:C_1210_3225Metric -> Capacitor_SMD:C_0603_1608Metric
- C10: value 100u -> 4u7; footprint Capacitor_SMD:C_1210_3225Metric -> Capacitor_SMD:C_0603_1608Metric
- C12, C15, C7, C8: value 100u -> 0u1; footprint Capacitor_SMD:C_1210_3225Metric -> Capacitor_SMD:C_0603_1608Metric
- C13: value 100u -> 1u; footprint Capacitor_SMD:C_1210_3225Metric -> Capacitor_SMD:C_0603_1608Metric
- C17, C2, C87, C91: value 100u -> 1u5; footprint Capacitor_SMD:C_1210_3225Metric -> Capacitor_SMD:C_0603_1608Metric
- C18: value 100n -> 1n; footprint Capacitor_SMD:C_0603_1608Metric -> Capacitor_SMD:C_0402_1005Metric
- C20, C27, C30, C32, C33, C74: value 100n -> 100u; footprint Capacitor_SMD:C_0603_1608Metric -> Capacitor_SMD:C_1210_3225Metric
- C21: value 5600pF -> 100u; footprint Capacitor_SMD:C_0603_1608Metric -> Capacitor_SMD:C_1210_3225Metric
- C22, C31: value 220u -> 100u; footprint ecocad_lib_footprints:CAP_EEE1HA221P -> Capacitor_SMD:C_1210_3225Metric
- C23: value 15pF -> 100u; footprint Capacitor_SMD:C_0603_1608Metric -> Capacitor_SMD:C_1210_3225Metric
- C24: value 150pF -> 100u; footprint Capacitor_SMD:C_0603_1608Metric -> Capacitor_SMD:C_1210_3225Metric
- C25: value 100n -> 1u
- C26: value 220u -> 100n; footprint ecocad_lib_footprints:CAP_EEE1HA221P -> Capacitor_SMD:C_0603_1608Metric
- C28: value 1800pF -> 100u; footprint Capacitor_SMD:C_0603_1608Metric -> Capacitor_SMD:C_1210_3225Metric
- C29: value 100n -> 47n
- C3, C88, C92: value 100u -> 1n; footprint Capacitor_SMD:C_1210_3225Metric -> Capacitor_SMD:C_0402_1005Metric
- C34, C35, C39: value 0u1 -> 100u; footprint Capacitor_SMD:C_0603_1608Metric -> Capacitor_SMD:C_1210_3225Metric
- C36, C37: value 4u7 -> 100u; footprint Capacitor_SMD:C_0603_1608Metric -> Capacitor_SMD:C_1210_3225Metric
- C40: value 1u -> 5600pF
- C42: value 0u1 -> 220u; footprint Capacitor_SMD:C_0603_1608Metric -> ecocad_lib_footprints:CAP_EEE1HA221P
- C43, C78: value 100u -> 150pF; footprint Capacitor_SMD:C_1210_3225Metric -> Capacitor_SMD:C_0603_1608Metric
- C44, C79: value 100u -> 15pF; footprint Capacitor_SMD:C_1210_3225Metric -> Capacitor_SMD:C_0603_1608Metric
- C5, C82: value 1u -> 100n
- C75: value 1u5 -> 5600pF
- C76: value 1n -> 100n; footprint Capacitor_SMD:C_0402_1005Metric -> Capacitor_SMD:C_0603_1608Metric
- C77: value 100n -> 220u; footprint Capacitor_SMD:C_0603_1608Metric -> ecocad_lib_footprints:CAP_EEE1HA221P
- C81: value 100u -> 220u; footprint Capacitor_SMD:C_1210_3225Metric -> ecocad_lib_footprints:CAP_EEE1HA221P
- C83: value 100n -> 1800pF
- C86: value 47n -> 100n
- C9: value 47n -> 4u7
- D1: value AMBER -> MMSZ5226B-7-F; footprint LED_SMD:LED_0805_2012Metric -> Diode_SMD:D_SOD-123
- D2: value RED -> MMSZ5226B-7-F; footprint LED_SMD:LED_0805_2012Metric -> Diode_SMD:D_SOD-123
- D3: value GREEN -> AMBER
- D4: value MMSZ5226B-7-F -> RED; footprint Diode_SMD:D_SOD-123 -> LED_SMD:LED_0805_2012Metric
- D5: value USBLC6-2SC6 -> GREEN; footprint Package_TO_SOT_SMD:TSOT-23-6_HandSoldering -> LED_SMD:LED_0805_2012Metric
- D6: value MMSZ5231B-7-F -> MMSZ5226B-7-F
- D7: value MMSZ5226B-7-F -> USBLC6-2SC6; footprint Diode_SMD:D_SOD-123 -> Package_TO_SOT_SMD:TSOT-23-6_HandSoldering
- D8: value MMSZ5226B-7-F -> MMSZ5231B-7-F
- R1: value 18.2k -> 220R; footprint Resistor_SMD:R_0603_1608Metric -> Resistor_SMD:R_0805_2012Metric
- R11: value 10k -> 18.2k
- R12: value 0 -> 250k
- R13: value 14k -> 10k
- R14: value 1.00k -> 46.4k
- R15: value 49.9 -> 10k
- R16: value 220R -> 20.0k; footprint Resistor_SMD:R_0805_2012Metric -> Resistor_SMD:R_0603_1608Metric
- R17: value 220R -> 2.2; footprint Resistor_SMD:R_0805_2012Metric -> Resistor_SMD:R_0603_1608Metric
- R18: value 220R -> 680R; footprint Resistor_SMD:R_0805_2012Metric -> Resistor_SMD:R_0603_1608Metric
- R19: value R -> 0
- R2: value 250k -> 220R; footprint Resistor_SMD:R_0603_1608Metric -> Resistor_SMD:R_0805_2012Metric
- R20: value 5.1k -> 10k; footprint Resistor_SMD:R_0805_2012Metric -> Resistor_SMD:R_0603_1608Metric
- R21: value 5.1k -> 0; footprint Resistor_SMD:R_0805_2012Metric -> Resistor_SMD:R_0603_1608Metric
- R3: value 10k -> 220R; footprint Resistor_SMD:R_0603_1608Metric -> Resistor_SMD:R_0805_2012Metric
- R4: value 46.4k -> R
- R5: value 10k -> 5.1k; footprint Resistor_SMD:R_0603_1608Metric -> Resistor_SMD:R_0805_2012Metric
- R6: value 20.0k -> 5.1k; footprint Resistor_SMD:R_0603_1608Metric -> Resistor_SMD:R_0805_2012Metric
- U1: value LM5145 -> ACS723xLCTR-10AU; footprint Package_DFN_QFN:Texas_RGY_R-PVQFN-N20_EP2.05x3.05mm_ThermalVias -> Package_SO:SOIC-8_3.9x4.9mm_P1.27mm
- U10: value MCP9700AT-ETT -> ACS723xLCTR-10AU; footprint Package_TO_SOT_SMD:SOT-23 -> Package_SO:SOIC-8_3.9x4.9mm_P1.27mm
- U11: value MCP9700AT-ETT -> MCP6007; footprint Package_TO_SOT_SMD:SOT-23 -> Package_SO:SOIC-8_3.9x4.9mm_P1.27mm
- U12: value MCP9700AT-ETT -> LM5145; footprint Package_TO_SOT_SMD:SOT-23 -> Package_DFN_QFN:Texas_RGY_R-PVQFN-N20_EP2.05x3.05mm_ThermalVias
- U19: value LM5145 -> MCP6007; footprint Package_DFN_QFN:Texas_RGY_R-PVQFN-N20_EP2.05x3.05mm_ThermalVias -> Package_SO:SOIC-8_3.9x4.9mm_P1.27mm
- U2, U20: value NTMFS4D0N08XT1G -> MCP6007; footprint ecocad_lib_footprints:PowerMosDFNHybrid -> Package_SO:SOIC-8_3.9x4.9mm_P1.27mm
- U21: value NTMFS4D0N08XT1G -> LM5145; footprint ecocad_lib_footprints:PowerMosDFNHybrid -> Package_DFN_QFN:Texas_RGY_R-PVQFN-N20_EP2.05x3.05mm_ThermalVias
- U3: value NTMFS4D0N08XT1G -> 8MHz; footprint ecocad_lib_footprints:PowerMosDFNHybrid -> Crystal:Crystal_SMD_3225-4Pin_3.2x2.5mm
- U4: value NTMFS4D0N08XT1G -> ~; footprint ecocad_lib_footprints:PowerMosDFNHybrid -> ecocad_lib_footprints:DB7W2-Female
- U5: value NTMFS4D0N08XT1G -> STM32G491KEUx; footprint ecocad_lib_footprints:PowerMosDFNHybrid -> Package_DFN_QFN:QFN-32-1EP_5x5mm_P0.5mm_EP3.45x3.45mm
- U6: value 8MHz -> MCP2542FD-E/SN; footprint Crystal:Crystal_SMD_3225-4Pin_3.2x2.5mm -> Package_SO:SOIC-8_3.9x4.9mm_P1.27mm
- U7: value ~ -> MCP9700AT-ETT; footprint ecocad_lib_footprints:DB7W2-Female -> Package_TO_SOT_SMD:SOT-23
- U8: value STM32G491KEUx -> MCP9700AT-ETT; footprint Package_DFN_QFN:QFN-32-1EP_5x5mm_P0.5mm_EP3.45x3.45mm -> Package_TO_SOT_SMD:SOT-23
- U9: value MCP2542FD-E/SN -> MCP9700AT-ETT; footprint Package_SO:SOIC-8_3.9x4.9mm_P1.27mm -> Package_TO_SOT_SMD:SOT-23
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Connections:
- C1 pad 1: /DC-DC-Converters/24V - 7V Converter/POWER_IN -> /DC-DC-Converters/Power Sensor VI1/SENSOR_VCC
- C1 pad 2: GND -> /DC-DC-Converters/Power Sensor VI1/SENSOR_GND
- C10 pad 1: /DC-DC-Converters/24V - 7V Converter/Output -> +3.3VA
- C10 pad 2: GND -> unconnected-(C10-Pad2)
- C11 pad 1: /DC-DC-Converters/24V - 7V Converter/POWER_IN -> GND
- C11 pad 2: GND -> +5V
- C12 pad 1: /DC-DC-Converters/24V - 7V Converter/Output -> +3.3VA
- C13 pad 1: /DC-DC-Converters/24V - 7V Converter/POWER_IN -> +3.3VA
- C14 pad 1: /DC-DC-Converters/24V - 7V Converter/Output -> GND
- C14 pad 2: GND -> +3V3
- C15 pad 1: /DC-DC-Converters/24V - 7V Converter/POWER_IN -> +3V3
- C16 pad 1: /DC-DC-Converters/24V - 7V Converter/POWER_IN -> /DC-DC-Converters/Power Sensor VI2/SENSOR_VCC
- C16 pad 2: GND -> /DC-DC-Converters/Power Sensor VI2/SENSOR_GND
- C17 pad 1: /DC-DC-Converters/24V - 7V Converter/Output -> /DC-DC-Converters/OUT_{12V}
- C17 pad 2: GND -> /DC-DC-Converters/Power Sensor VI2/SENSOR_GND
- C18 pad 1: /DC-DC-Converters/24V - 7V Converter/POWER_IN -> Net-(D10-K)
- C18 pad 2: GND -> /DC-DC-Converters/Power Sensor VI2/SENSOR_GND
- C19 pad 1: /DC-DC-Converters/24V - 7V Converter/Output -> /DC-DC-Converters/Power Sensor VI2/SENSOR_VCC
- C19 pad 2: GND -> /DC-DC-Converters/Power Sensor VI2/SENSOR_GND
- C2 pad 1: /DC-DC-Converters/24V - 7V Converter/POWER_IN -> /DC-DC-Converters/DC-DC-Buck-Converter/POWER_IN
- C2 pad 2: GND -> /DC-DC-Converters/Power Sensor VI1/SENSOR_GND
- C20 pad 1: /DC-DC-Converters/24V - 7V Converter/POWER_IN -> /DC-DC-Converters/DC-DC-Buck-Converter1/POWER_IN
- C21 pad 1: Net-(U1-COMP) -> /DC-DC-Converters/DC-DC-Buck-Converter1/Output
- C21 pad 2: Net-(C21-Pad2) -> GND
- C22 pad 1: /DC-DC-Converters/24V - 7V Converter/Output -> /DC-DC-Converters/DC-DC-Buck-Converter1/POWER_IN
- C23 pad 1: GND -> /DC-DC-Converters/DC-DC-Buck-Converter1/Output
- C23 pad 2: Net-(U1-ILIM) -> GND
- C24 pad 1: Net-(U1-COMP) -> /DC-DC-Converters/DC-DC-Buck-Converter1/POWER_IN
- C24 pad 2: Net-(U1-FB) -> GND
- C25 pad 1: /DC-DC-Converters/24V - 7V Converter/POWER_IN -> GND
- C25 pad 2: GND -> Net-(U12-VCC)
- C26 pad 1: /DC-DC-Converters/24V - 7V Converter/Output -> GND
- C26 pad 2: GND -> Net-(U12-VIN)
- C27 pad 1: /DC-DC-Converters/24V - 7V Converter/POWER_IN -> /DC-DC-Converters/DC-DC-Buck-Converter1/Output
- C28 pad 1: Net-(U1-FB) -> /DC-DC-Converters/DC-DC-Buck-Converter1/POWER_IN
- C28 pad 2: Net-(C28-Pad2) -> GND
- C29 pad 1: /DC-DC-Converters/24V - 7V Converter/POWER_IN -> GND
- C29 pad 2: GND -> Net-(U12-SS_TRK)
- C3 pad 1: /DC-DC-Converters/24V - 7V Converter/Output -> Net-(D2-K)
- C3 pad 2: GND -> /DC-DC-Converters/Power Sensor VI1/SENSOR_GND
- C30 pad 1: Net-(U1-SW) -> /DC-DC-Converters/DC-DC-Buck-Converter1/Output
- C30 pad 2: Net-(U1-BST) -> GND
- C31 pad 1: /DC-DC-Converters/24V - 12V Converter/Output -> /DC-DC-Converters/DC-DC-Buck-Converter1/POWER_IN
- C32 pad 1: GNDA -> /DC-DC-Converters/DC-DC-Buck-Converter1/Output
- C32 pad 2: +3V3 -> GND
- C33 pad 1: GND -> /DC-DC-Converters/DC-DC-Buck-Converter1/POWER_IN
- C33 pad 2: /MCU and sensors/NRST -> GND
- C34 pad 1: +3V3 -> /DC-DC-Converters/DC-DC-Buck-Converter1/Output
- C34 pad 2: GNDA -> GND
- C35 pad 1: +3V3 -> /DC-DC-Converters/DC-DC-Buck-Converter1/POWER_IN
- C35 pad 2: GNDA -> GND
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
